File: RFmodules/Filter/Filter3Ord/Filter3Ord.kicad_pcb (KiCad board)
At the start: 2 copper layers, 38.1 x 8.3 mm, 9 parts, among them J1 SMA, J2 SMA

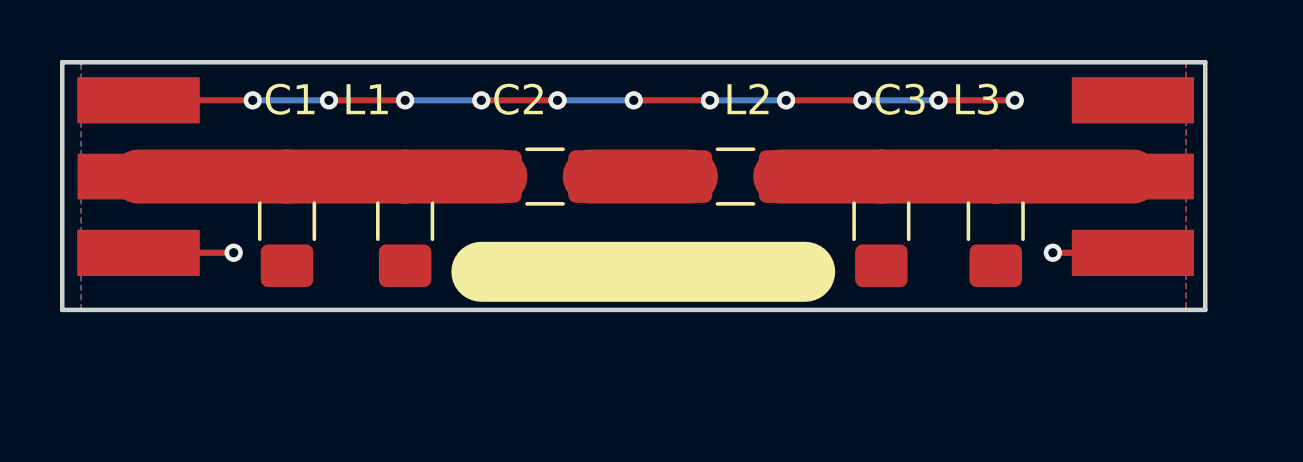
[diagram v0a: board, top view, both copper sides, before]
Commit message: Add bandpass filter 3 order 0402
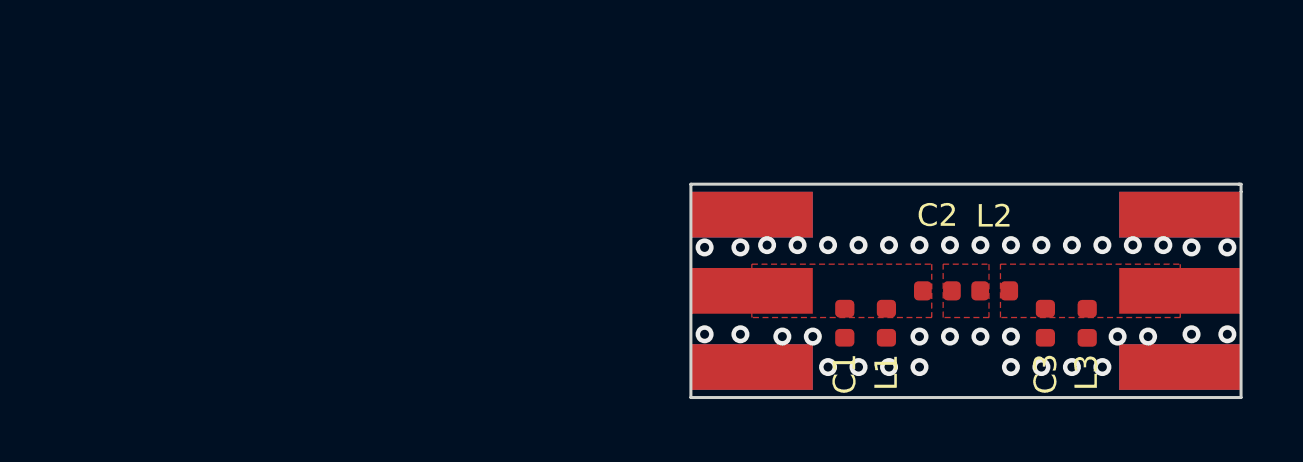
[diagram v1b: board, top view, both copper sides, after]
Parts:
- removed REF**: OSHW-Logo_5.7x6mm_SilkScreen, Symbol:OSHW-Logo_5.7x6mm_SilkScreen
- C1, C2, C3: footprint Capacitor_SMD:C_1206_3216Metric_Pad1.42x1.75mm_HandSolder -> Capacitor_SMD:C_0402_1005Metric
- L1, L2, L3: footprint Inductor_SMD:L_1206_3216Metric_Pad1.42x1.75mm_HandSolder -> Inductor_SMD:L_0402_1005Metric
- moved J1 20.8 mm to (137.2, 108.0)
- moved C1 18.9 mm to (142.3, 109.0)
- moved L1 16.4 mm to (143.7, 109.0)
- moved C2 13.6 mm to (145.4, 108.0)
- moved L2 9.44 mm to (147.3, 108.0)
- moved C3 6.44 mm to (149.0, 109.0)
- moved L3 4.57 mm to (150.4, 109.0)
- moved J2 4.12 mm to (151.4, 108.0)
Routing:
- net GND: track 35.1 -> 0.00 mm, vias 13 -> 38
- net Net-(C1-Pad1): track 12.1 -> 0.00 mm
- net Net-(C3-Pad1): track 11.8 -> 0.00 mm
- net Net-(C2-Pad1): track 3.38 -> 0.00 mm
- added copper zone on F.Cu, net Net-(C1-Pad1)
- added copper zone on F.Cu, net Net-(C2-Pad1)
- added copper zone on F.Cu, net Net-(C3-Pad1)
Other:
- board size 38.1 x 8.3 mm -> 18.3 x 7.1 mm
- net class 0402 added: clearance 0.1, trace_width 0.61, via_dia 0.6, via_drill 0.3
- net class 50 Ohm added: clearance 0.37, trace_width 1.8, via_dia 0.6, via_drill 0.3
- net class 50Ohm removed
- net class Default: clearance 0.2032 -> 0.2; trace_width 0.2032 -> 0.25; via_dia 0.6096 -> 0.6; via_drill 0.3048 -> 0.3
- rule pad_to_mask_clearance: 0.051 -> 0
- rule trace_clearance: 0.2032 -> 0.2
- rule trace_min: 0.2032 -> 0.2
- rule via_min_drill: 0.3048 -> 0.3
- rule via_min_size: 0.6096 -> 0.4
- board text added: "Bandpass Filter 3 Order Revision 0.1.0 - 01/2019 github.com/fgaletsee/RFLego"

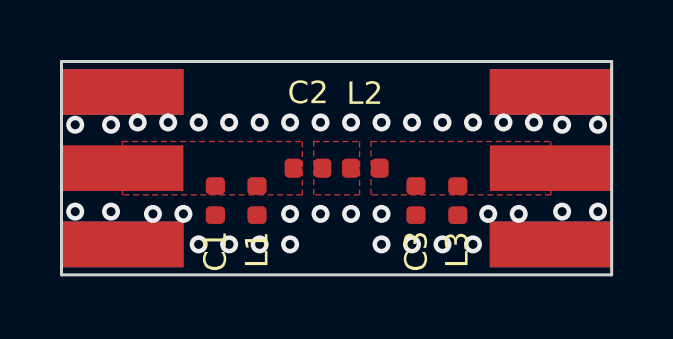
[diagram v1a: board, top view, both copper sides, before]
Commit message: Fix design guide issues and typos
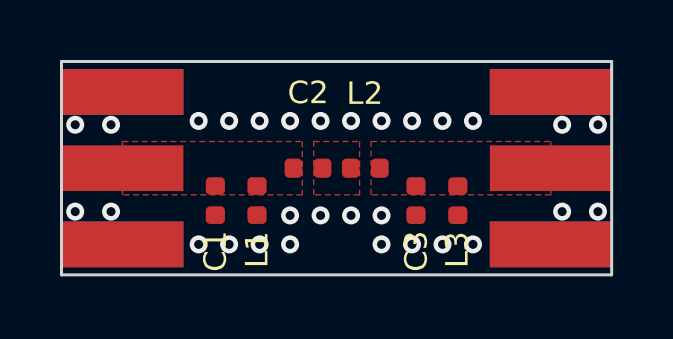
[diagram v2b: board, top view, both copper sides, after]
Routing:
- net GND: vias 38 -> 30
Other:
- board text added: "Bandpass Filter 3th Order Revision 0.1.0 - 01/2019 github.com/fgaletsee/RFLego"
- board text removed: "Bandpass Filter 3 Order Revision 0.1.0 - 01/2019 github.com/fgaletsee/RFLego"
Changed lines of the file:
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@@
     (thickness 1.6)
     (drawings 10)
-    (tracks 38)
+    (tracks 30)
     (zones 0)
     (modules 8)
@@
   (page A4)
   (layers
-    (0 F.Cu signal hide)
-    (31 B.Cu signal hide)
-    (32 B.Adhes user)
-    (33 F.Adhes user)
-    (34 B.Paste user)
-    (35 F.Paste user)
-    (36 B.SilkS user)
-    (37 F.SilkS user)
-    (38 B.Mask user)
+    (0 F.Cu signal)
+    (31 B.Cu signal)
+    (32 B.Adhes user hide)
+    (33 F.Adhes user hide)
+    (34 B.Paste user hide)
+    (35 F.Paste user hide)
+    (36 B.SilkS user hide)
+    (37 F.SilkS user hide)
+    (38 B.Mask user hide)
     (39 F.Mask user)
-    (40 Dwgs.User user)
-    (41 Cmts.User user)
-    (42 Eco1.User user)
-    (43 Eco2.User user)
-    (44 Edge.Cuts user)
-    (45 Margin user)
-    (46 B.CrtYd user)
-    (47 F.CrtYd user)
-    (48 B.Fab user)
-    (49 F.Fab user)
+    (40 Dwgs.User user hide)
+    (41 Cmts.User user hide)
+    (42 Eco1.User user hide)
+    (43 Eco2.User user hide)
+    (44 Edge.Cuts user hide)
+    (45 Margin user hide)
+    (46 B.CrtYd user hide)
+    (47 F.CrtYd user hide)
+    (48 B.Fab user hide)
+    (49 F.Fab user hide)
   )
   (setup
@@
   )
   (gr_line (start 150.3172 110.49) (end 142.4178 110.49) (layer B.SilkS) (width 1.5))
-  (gr_text "Bandpass Filter 3 Order\nRevision 0.1.0 - 01/2019\ngithub.com/fgaletsee/RFLego\n" (at 146.1516 107.95) (layer B.SilkS)
+  (gr_text "Bandpass Filter 3th Order\nRevision 0.1.0 - 01/2019\ngithub.com/fgaletsee/RFLego\n" (at 146.1516 107.95) (layer B.SilkS)
     (effects (font (size 0.6 0.6) (thickness 0.15)) (justify mirror))
   )
@@
   (via (at 141.732 110.49) (size 0.6) (drill 0.3) (layers F.Cu B.Cu) (net 2))
   (via (at 144.78 110.49) (size 0.6) (drill 0.3) (layers F.Cu B.Cu) (net 2))
-  (via (at 144.78 109.474) (size 0.6) (drill 0.3) (layers F.Cu B.Cu) (net 2))
-  (via (at 145.796 109.474) (size 0.6) (drill 0.3) (layers F.Cu B.Cu) (net 2))
-  (via (at 146.812 109.474) (size 0.6) (drill 0.3) (layers F.Cu B.Cu) (net 2))
-  (via (at 147.828 109.474) (size 0.6) (drill 0.3) (layers F.Cu B.Cu) (net 2))
+  (via (at 144.78 109.5248) (size 0.6) (drill 0.3) (layers F.Cu B.Cu) (net 2))
+  (via (at 145.796 109.5248) (size 0.6) (drill 0.3) (layers F.Cu B.Cu) (net 2))
+  (via (at 146.812 109.5248) (size 0.6) (drill 0.3) (layers F.Cu B.Cu) (net 2))
+  (via (at 147.828 109.5248) (size 0.6) (drill 0.3) (layers F.Cu B.Cu) (net 2))
   (via (at 147.828 110.49) (size 0.6) (drill 0.3) (layers F.Cu B.Cu) (net 2))
   (via (at 148.844 110.49) (size 0.6) (drill 0.3) (layers F.Cu B.Cu) (net 2))
@@
   (via (at 150.876 110.49) (size 0.6) (drill 0.3) (layers F.Cu B.Cu) (net 2))
   (via (at 143.764 110.49) (size 0.6) (drill 0.3) (layers F.Cu B.Cu) (net 2))
-  (via (at 141.732 106.426) (size 0.6) (drill 0.3) (layers F.Cu B.Cu) (net 2))
-  (via (at 142.748 106.426) (size 0.6) (drill 0.3) (layers F.Cu B.Cu) (net 2))
-  (via (at 143.764 106.426) (size 0.6) (drill 0.3) (layers F.Cu B.Cu) (net 2))
-  (via (at 144.78 106.426) (size 0.6) (drill 0.3) (layers F.Cu B.Cu) (net 2))
-  (via (at 145.796 106.426) (size 0.6) (drill 0.3) (layers F.Cu B.Cu) (net 2))
-  (via (at 146.812 106.426) (size 0.6) (drill 0.3) (layers F.Cu B.Cu) (net 2))
-  (via (at 147.828 106.426) (size 0.6) (drill 0.3) (layers F.Cu B.Cu) (net 2))
-  (via (at 148.844 106.426) (size 0.6) (drill 0.3) (layers F.Cu B.Cu) (net 2))
-  (via (at 149.86 106.426) (size 0.6) (drill 0.3) (layers F.Cu B.Cu) (net 2))
-  (via (at 150.876 106.426) (size 0.6) (drill 0.3) (layers F.Cu B.Cu) (net 2))
+  (via (at 141.732 106.3752) (size 0.6) (drill 0.3) (layers F.Cu B.Cu) (net 2))
+  (via (at 142.748 106.3752) (size 0.6) (drill 0.3) (layers F.Cu B.Cu) (net 2))
+  (via (at 143.764 106.3752) (size 0.6) (drill 0.3) (layers F.Cu B.Cu) (net 2))
+  (via (at 144.78 106.3752) (size 0.6) (drill 0.3) (layers F.Cu B.Cu) (net 2))
+  (via (at 145.796 106.3752) (size 0.6) (drill 0.3) (layers F.Cu B.Cu) (net 2))
+  (via (at 146.812 106.3752) (size 0.6) (drill 0.3) (layers F.Cu B.Cu) (net 2))
+  (via (at 147.828 106.3752) (size 0.6) (drill 0.3) (layers F.Cu B.Cu) (net 2))
+  (via (at 148.844 106.3752) (size 0.6) (drill 0.3) (layers F.Cu B.Cu) (net 2))
+  (via (at 149.86 106.3752) (size 0.6) (drill 0.3) (layers F.Cu B.Cu) (net 2))
+  (via (at 150.876 106.3752) (size 0.6) (drill 0.3) (layers F.Cu B.Cu) (net 2))
   (via (at 155.0416 106.5022) (size 0.6) (drill 0.3) (layers F.Cu B.Cu) (net 2))
   (via (at 155.0416 109.3978) (size 0.6) (drill 0.3) (layers F.Cu B.Cu) (net 2))
@@
   (via (at 153.8478 106.5022) (size 0.6) (drill 0.3) (layers F.Cu B.Cu) (net 2))
   (via (at 153.8478 109.3978) (size 0.6) (drill 0.3) (layers F.Cu B.Cu) (net 2))
-  (via (at 141.224 109.474) (size 0.6) (drill 0.3) (layers F.Cu B.Cu) (net 2))
-  (via (at 140.208 109.474) (size 0.6) (drill 0.3) (layers F.Cu B.Cu) (net 2))
-  (via (at 140.716 106.426) (size 0.6) (drill 0.3) (layers F.Cu B.Cu) (net 2))
-  (via (at 139.7 106.426) (size 0.6) (drill 0.3) (layers F.Cu B.Cu) (net 2))
-  (via (at 151.892 106.426) (size 0.6) (drill 0.3) (layers F.Cu B.Cu) (net 2))
-  (via (at 152.908 106.426) (size 0.6) (drill 0.3) (layers F.Cu B.Cu) (net 2))
-  (via (at 151.384 109.474) (size 0.6) (drill 0.3) (layers F.Cu B.Cu) (net 2))
-  (via (at 152.4 109.474) (size 0.6) (drill 0.3) (layers F.Cu B.Cu) (net 2))
   (zone (net 1) (net_name "Net-(C1-Pad1)") (layer F.Cu) (hatch edge 0.508)
     (priority 1)
@@
       )
     )
-  )
-  (zone (net 2) (net_name GND) (layer B.Cu) (hatch edge 0.508)
-    (connect_pads yes (clearance 0.1))
-    (min_thickness 0.1)
-    (fill yes (arc_segments 16) (thermal_gap 0.508) (thermal_bridge_width 0.508))
-    (polygon
-      (pts
-        (xy 137.16 104.394) (xy 155.4988 104.394) (xy 155.4988 111.506) (xy 137.16 111.506)
-      )
-    )

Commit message: Update board descriptions, add Bandstop elliptic filter 5th order
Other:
- board text added: "Bandpass Filter 3th Order Revision 1 - 01/2019 github.com/fgaletsee/RFLego"
- board text removed: "Bandpass Filter 3th Order Revision 0.1.0 - 01/2019 github.com/fgaletsee/RFLego"
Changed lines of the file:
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@@
     (0 F.Cu signal)
     (31 B.Cu signal)
-    (32 B.Adhes user hide)
-    (33 F.Adhes user hide)
-    (34 B.Paste user hide)
-    (35 F.Paste user hide)
-    (36 B.SilkS user hide)
-    (37 F.SilkS user hide)
-    (38 B.Mask user hide)
+    (32 B.Adhes user)
+    (33 F.Adhes user)
+    (34 B.Paste user)
+    (35 F.Paste user)
+    (36 B.SilkS user)
+    (37 F.SilkS user)
+    (38 B.Mask user)
     (39 F.Mask user)
-    (40 Dwgs.User user hide)
-    (41 Cmts.User user hide)
-    (42 Eco1.User user hide)
-    (43 Eco2.User user hide)
-    (44 Edge.Cuts user hide)
-    (45 Margin user hide)
-    (46 B.CrtYd user hide)
-    (47 F.CrtYd user hide)
-    (48 B.Fab user hide)
-    (49 F.Fab user hide)
+    (40 Dwgs.User user)
+    (41 Cmts.User user)
+    (42 Eco1.User user)
+    (43 Eco2.User user)
+    (44 Edge.Cuts user)
+    (45 Margin user)
+    (46 B.CrtYd user)
+    (47 F.CrtYd user)
+    (48 B.Fab user)
+    (49 F.Fab user)
   )
   (setup
@@
   )
   (gr_line (start 150.3172 110.49) (end 142.4178 110.49) (layer B.SilkS) (width 1.5))
-  (gr_text "Bandpass Filter 3th Order\nRevision 0.1.0 - 01/2019\ngithub.com/fgaletsee/RFLego\n" (at 146.1516 107.95) (layer B.SilkS)
+  (gr_text "Bandpass Filter 3th Order\nRevision 1 - 01/2019\ngithub.com/fgaletsee/RFLego\n" (at 146.1516 107.95) (layer B.SilkS)
     (effects (font (size 0.6 0.6) (thickness 0.15)) (justify mirror))
   )
